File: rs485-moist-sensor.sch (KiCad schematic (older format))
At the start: 27 parts, among them IC1 ATTINY441-SSU, P1 CONN_02X03, P2 CONN_01X04, Q1 Q_PMOS_GSD, U1 SN65HVD72, U2 MCP1702, X1 16MHz

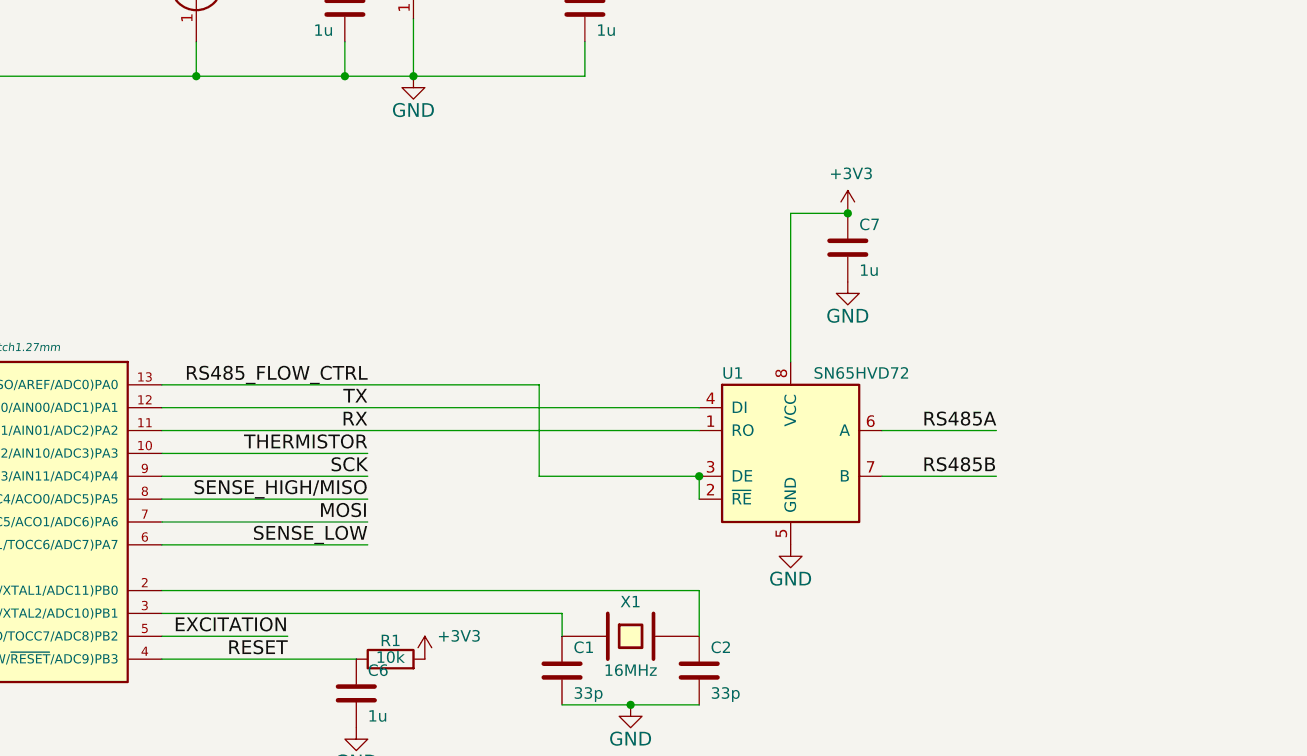
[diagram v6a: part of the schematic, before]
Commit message: Add a pulldown resistor to make transceiver more robust
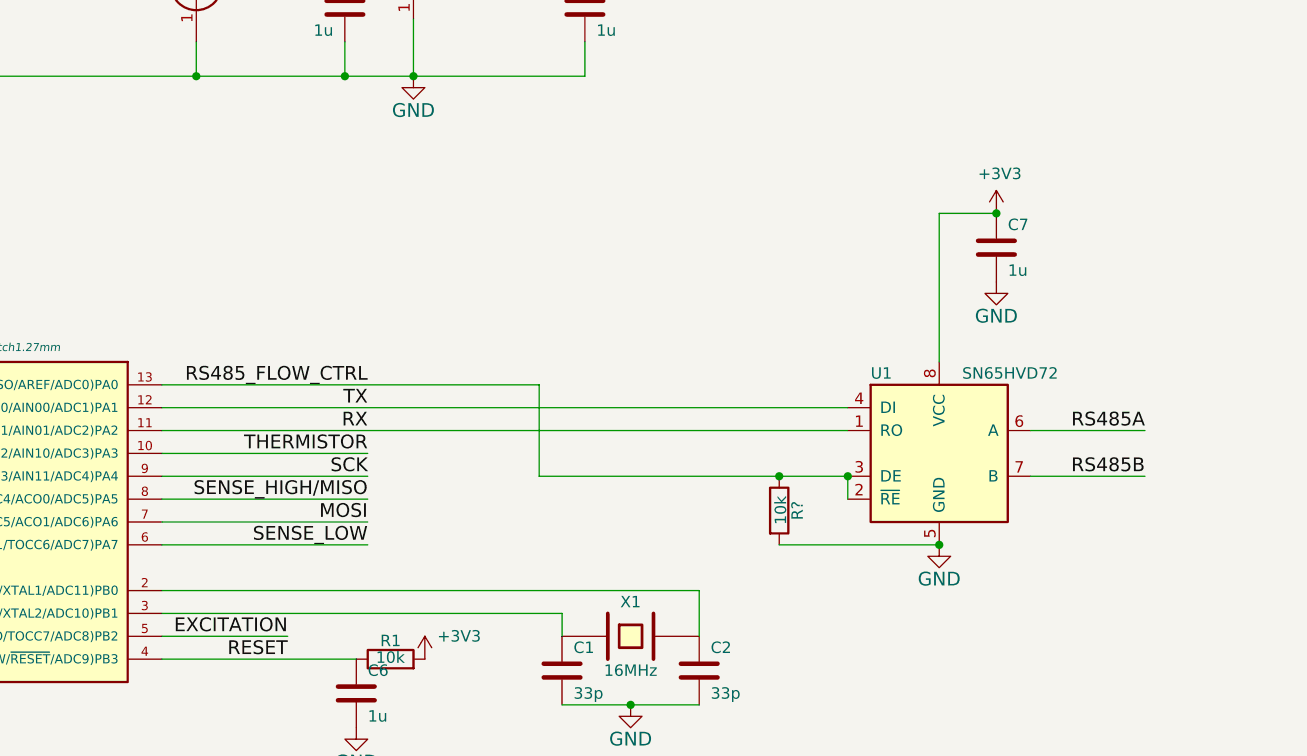
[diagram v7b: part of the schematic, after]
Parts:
- added R?: 10k, Resistors_SMD:R_0603, symbol R
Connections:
- net GND: now also R?.2
- net RS485_FLOW_CTRL: now also R?.1
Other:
- moved on the sheet: C7, U1
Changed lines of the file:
@@
 L SP3481EN-RESCUE-rs485-moist-sensor U1
 U 1 1 54DF0ADA
-P 5750 3600
-F 0 "U1" H 5450 3950 50  0000 L CNN
-F 1 "SN65HVD72" H 5850 3950 50  0000 L CNN
-F 2 "Housings_SOIC:SOIC-8_3.9x4.9mm_Pitch1.27mm" H 5750 3600 50  0001 C CIN
-F 3 "" H 5750 3600 60  0000 C CNN
-F 4 "SN65HVD72DR" H 5750 3600 60  0001 C CNN "PartNo"
-F 5 "TEXAS INSTRUMENTS" H 5750 3600 60  0001 C CNN "Manufacturer"
-F 6 "2542747" H 5750 3600 60  0001 C CNN "Distributor"
-	1    5750 3600
+P 6400 3600
+F 0 "U1" H 6100 3950 50  0000 L CNN
+F 1 "SN65HVD72" H 6500 3950 50  0000 L CNN
+F 2 "Housings_SOIC:SOIC-8_3.9x4.9mm_Pitch1.27mm" H 6400 3600 50  0001 C CIN
+F 3 "" H 6400 3600 60  0000 C CNN
+F 4 "SN65HVD72DR" H 6400 3600 60  0001 C CNN "PartNo"
+F 5 "TEXAS INSTRUMENTS" H 6400 3600 60  0001 C CNN "Manufacturer"
+F 6 "2542747" H 6400 3600 60  0001 C CNN "Distributor"
+	1    6400 3600
 	1    0    0    -1
 $EndComp
@@
 L C C7
 U 1 1 54DF0C76
-P 6000 2700
-F 0 "C7" H 6050 2800 50  0000 L CNN
-F 1 "1u" H 6050 2600 50  0000 L CNN
-F 2 "Capacitors_SMD:C_0603" H 6038 2550 30  0001 C CNN
-F 3 "" H 6000 2700 60  0000 C CNN
-	1    6000 2700
+P 6650 2700
+F 0 "C7" H 6700 2800 50  0000 L CNN
+F 1 "1u" H 6700 2600 50  0000 L CNN
+F 2 "Capacitors_SMD:C_0603" H 6688 2550 30  0001 C CNN
+F 3 "" H 6650 2700 60  0000 C CNN
+	1    6650 2700
 	1    0    0    -1
 $EndComp
@@
 L GND #PWR08
 U 1 1 54DF0CCD
-P 6000 2850
-F 0 "#PWR08" H 6000 2600 60  0001 C CNN
-F 1 "GND" H 6000 2700 60  0000 C CNN
-F 2 "" H 6000 2850 60  0000 C CNN
-F 3 "" H 6000 2850 60  0000 C CNN
-	1    6000 2850
+P 6650 2850
+F 0 "#PWR08" H 6650 2600 60  0001 C CNN
+F 1 "GND" H 6650 2700 60  0000 C CNN
+F 2 "" H 6650 2850 60  0000 C CNN
+F 3 "" H 6650 2850 60  0000 C CNN
+	1    6650 2850
 	1    0    0    -1
 $EndComp
@@
 L GND #PWR09
 U 1 1 54DF15E6
-P 5750 4000
-F 0 "#PWR09" H 5750 3750 60  0001 C CNN
-F 1 "GND" H 5750 3850 60  0000 C CNN
-F 2 "" H 5750 4000 60  0000 C CNN
-F 3 "" H 5750 4000 60  0000 C CNN
-	1    5750 4000
+P 6400 4000
+F 0 "#PWR09" H 6400 3750 60  0001 C CNN
+F 1 "GND" H 6400 3850 60  0000 C CNN
+F 2 "" H 6400 4000 60  0000 C CNN
+F 3 "" H 6400 4000 60  0000 C CNN
+	1    6400 4000
 	1    0    0    -1
 $EndComp
@@
 Text Label 3900 3600 2    60   ~ 0
 THERMISTOR
-Text Label 6650 3500 2    60   ~ 0
+Text Label 7300 3500 2    60   ~ 0
 RS485A
-Text Label 6650 3700 2    60   ~ 0
+Text Label 7300 3700 2    60   ~ 0
 RS485B
 Wire Wire Line
@@
 	8950 4500 8950 4900
 Wire Wire Line
-	5750 3200 5750 2550
-Wire Wire Line
-	5750 2550 6000 2550
+	6400 3200 6400 2550
+Wire Wire Line
+	6400 2550 6650 2550
 Wire Wire Line
 	3000 4200 5350 4200
@@
 	3000 4000 3900 4000
 Wire Wire Line
-	6150 3500 6650 3500
+	6800 3500 7300 3500
 Wire Wire Line
 	9700 1850 8700 1850
 Wire Wire Line
-	3000 3500 5350 3500
-Wire Wire Line
-	3000 3400 5350 3400
-Connection ~ 5350 3700
-Wire Wire Line
-	5350 3700 5350 3800
-Wire Wire Line
-	5350 3700 4650 3700
+	3000 3500 6000 3500
+Wire Wire Line
+	3000 3400 6000 3400
+Connection ~ 6000 3700
+Wire Wire Line
+	6000 3700 6000 3800
+Wire Wire Line
+	6000 3700 4650 3700
 Wire Wire Line
 	4650 3700 4650 3300
@@
 L +3V3 #PWR018
 U 1 1 58946C25
-P 6000 2550
-F 0 "#PWR018" H 3200 1600 50  0001 C CNN
-F 1 "+3V3" H 6015 2723 50  0000 C CNN
-F 2 "" H 3200 1750 60  0000 C CNN
-F 3 "" H 3200 1750 60  0000 C CNN
-	1    6000 2550
-	1    0    0    -1
-$EndComp
-Connection ~ 6000 2550
+P 6650 2550
+F 0 "#PWR018" H 3850 1600 50  0001 C CNN
+F 1 "+3V3" H 6665 2723 50  0000 C CNN
+F 2 "" H 3850 1750 60  0000 C CNN
+F 3 "" H 3850 1750 60  0000 C CNN
+	1    6650 2550
+	1    0    0    -1
+$EndComp
+Connection ~ 6650 2550
 $Comp
 L +3V3 #PWR019
@@
 Connection ~ 3150 1950
 Wire Wire Line
-	6150 3700 6650 3700
+	6800 3700 7300 3700
 $Comp
 L TVS-ARRAY D4
@@
 	1    0    0    -1
 $EndComp
+$Comp
+L R R?
+U 1 1 58FEF0D0
+P 5700 3850
+F 0 "R?" V 5780 3850 50  0000 C CNN
+F 1 "10k" V 5707 3851 50  0000 C CNN
+F 2 "Resistors_SMD:R_0603" V 5630 3850 30  0001 C CNN
+F 3 "" H 5700 3850 30  0000 C CNN
+	1    5700 3850
+	1    0    0    -1
+$EndComp
+Wire Wire Line
+	6400 4000 5700 4000
+Connection ~ 6400 4000
+Connection ~ 5700 3700
 $EndSCHEMATC

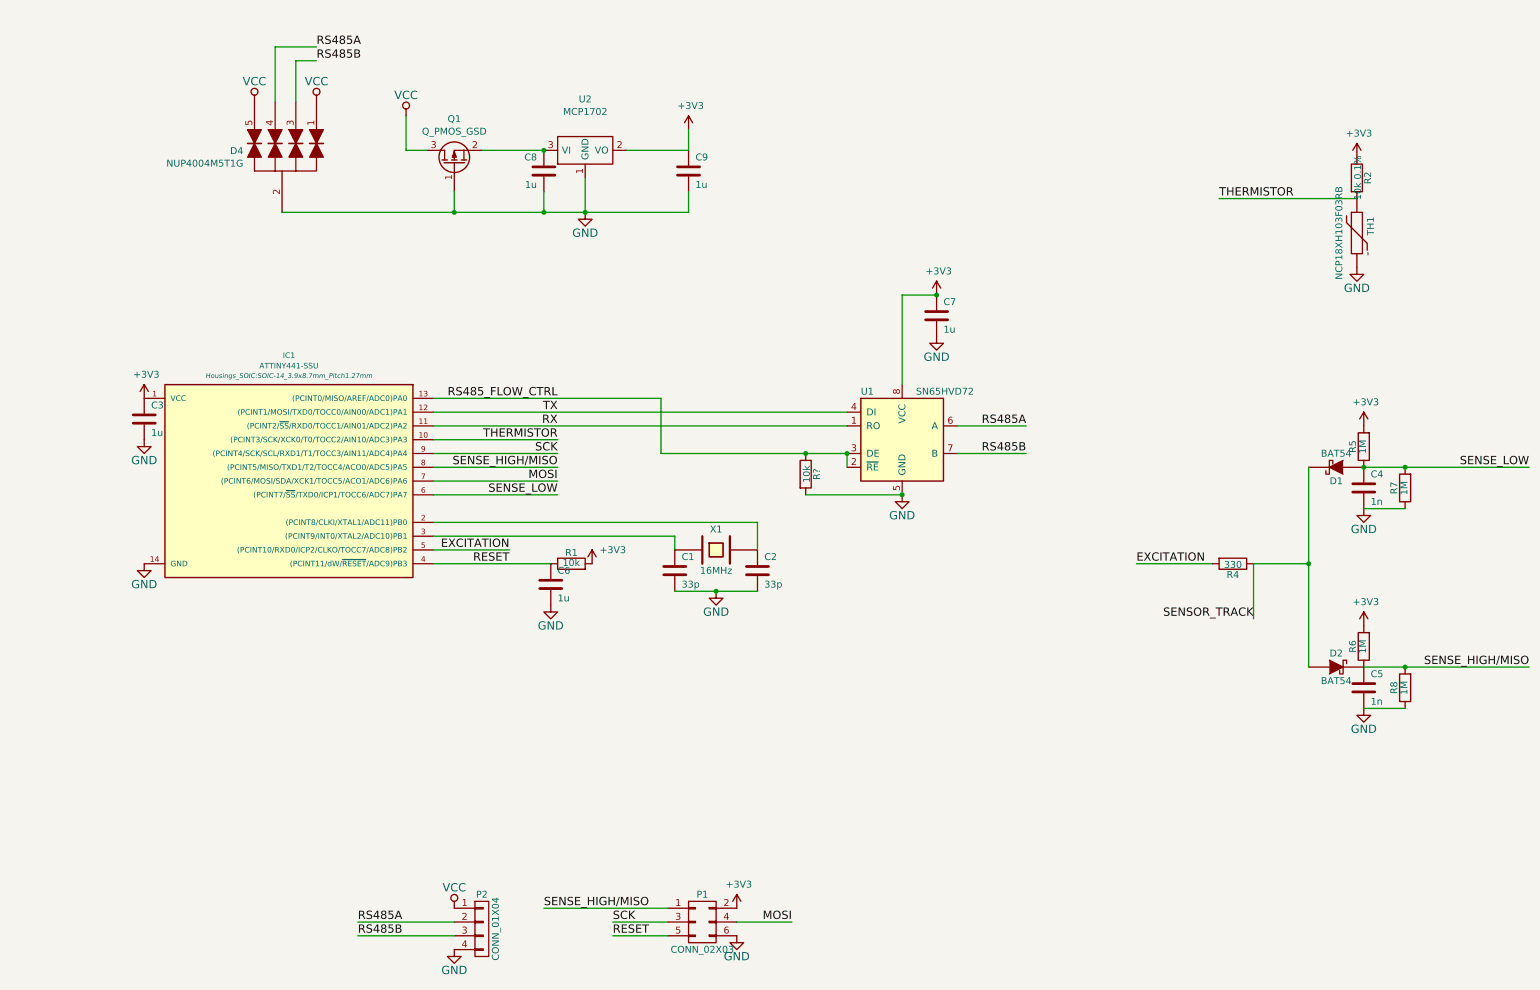
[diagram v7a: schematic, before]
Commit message: Pullup/pulldown resistors to put rs485 transceiver in off mode by default. Connect DE, ~RE lines to MCU separately. Provide power to resistive dividers from MCU, not from regulator to allow for lower power consumption
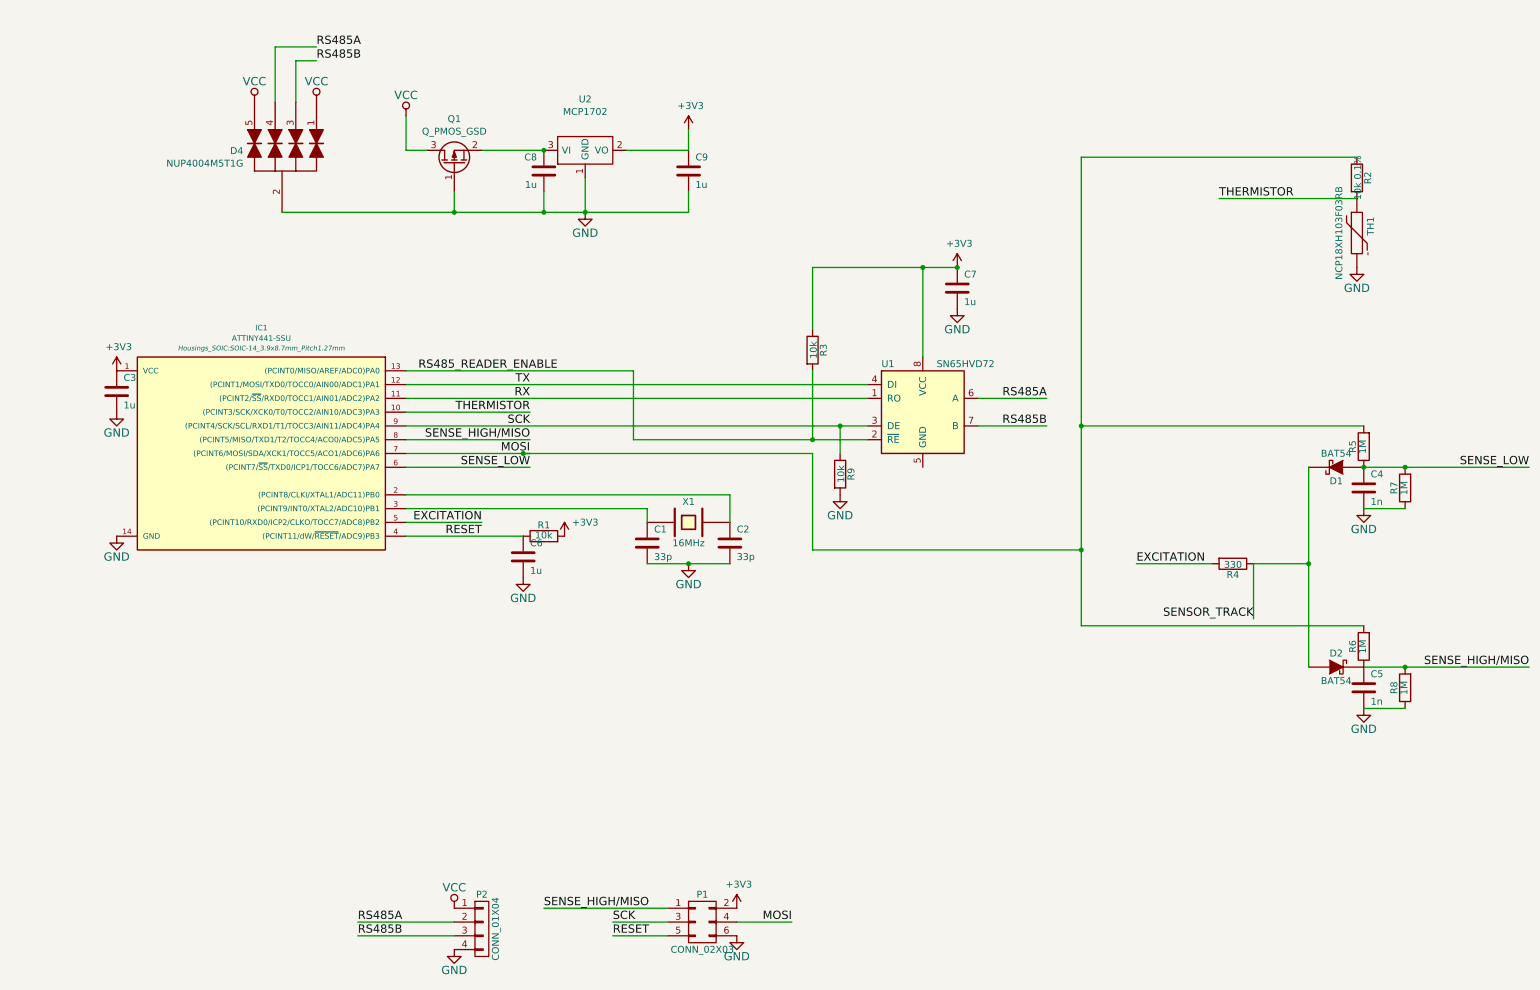
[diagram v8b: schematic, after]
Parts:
- added R3: 10k, Resistors_SMD:R_0603, symbol R
- gave numbers to parts that had none: 1
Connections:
- net +3V3: now also R3.1; no longer R2.1, R5.2, R6.2
- net GND: no longer U1.5 (GND)
- net MOSI: now also R2.1, R5.2, R6.2
- net SCK: now also R9.1, U1.3 (DE)
- net RS485_FLOW_CTRL renamed RS485_READER_ENABLE
- net RS485_READER_ENABLE: now also R3.2; no longer R9.1, U1.3 (DE)
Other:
- moved on the sheet: C1, C2, C3, C6, C7, IC1, R1, R9, U1, X1
